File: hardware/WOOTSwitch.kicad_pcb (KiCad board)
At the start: 2 copper layers, 100 x 88 mm, 133 parts, among them J1 Mini-DIN-4-G, J10 POWSEL, J11 TWI, J12 TWI, J13 Mini-DIN-4-G, J14 Mini-DIN-4-G, J15 Mini-DIN-4-G, J16 Mini-DIN-4-G, J2 Mini-DIN-4-G, J7 Barrel_Jack_MountingPin, J8 EXT_POW, J9 SW1, Q1 MMBT3904, Q11 2N7002, Q15 2N7002, Q17 2N7002, Q18 2N7002, Q19 2N7002, Q2 MMBT3904, Q20 2N7002, Q21 2N7002, Q22 2N7002, Q23 2N7002, Q24 2N7002, Q25 2N7002, Q26 2N7002, Q27 2N7002, Q28 2N7002, Q29 2N7002, Q3 MMBT3904, Q30 2N7002, Q31 2N7002, Q32 2N7002, Q33 2N7002, Q34 2N7002, Q35 2N7002, Q36 2N7002, Q37 2N7002, Q38 2N7002, Q39 2N7002, Q4 MMBT3904, Q40 2N7002, Q5 MMBT3904, Q6 MMBT3904, Q8 MMBT3904, Q9 2N7002, SW2 1825910-6, U1 Pico, U2 LM1117-5.0

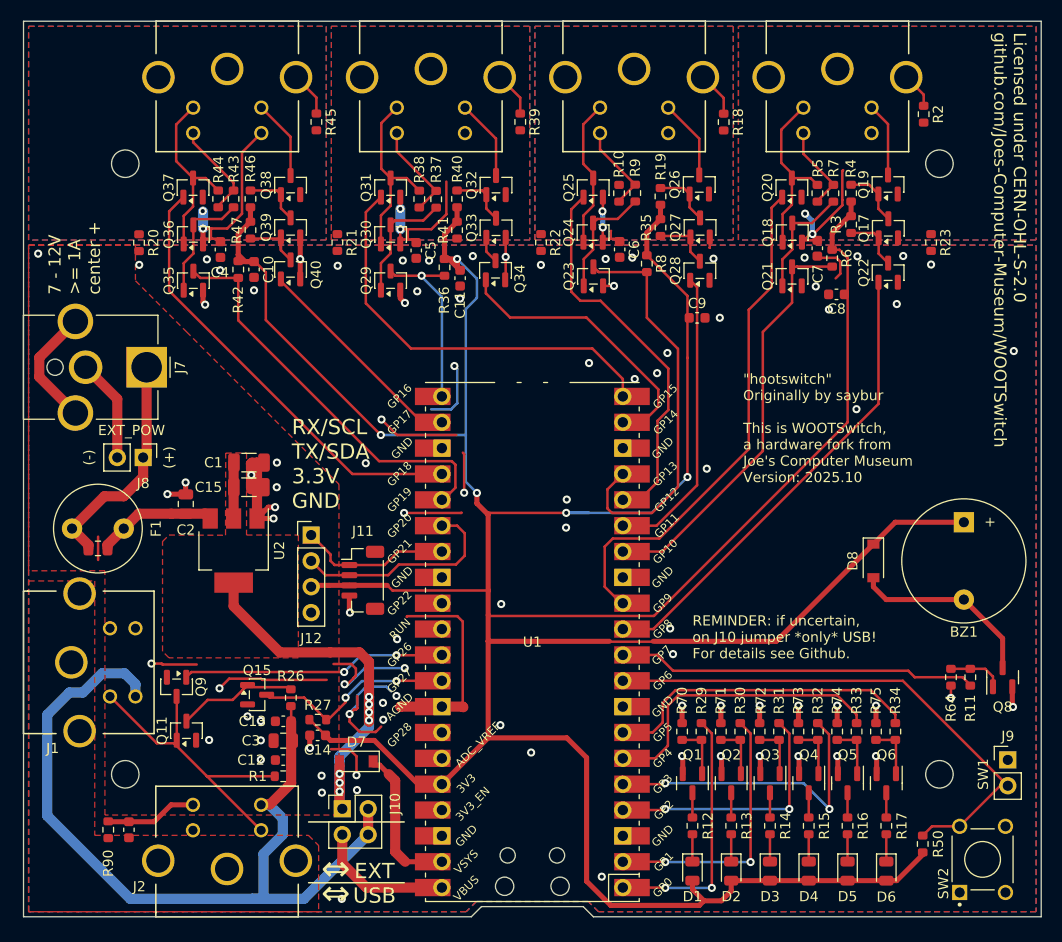
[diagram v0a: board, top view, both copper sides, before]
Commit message: Moved mounting holes
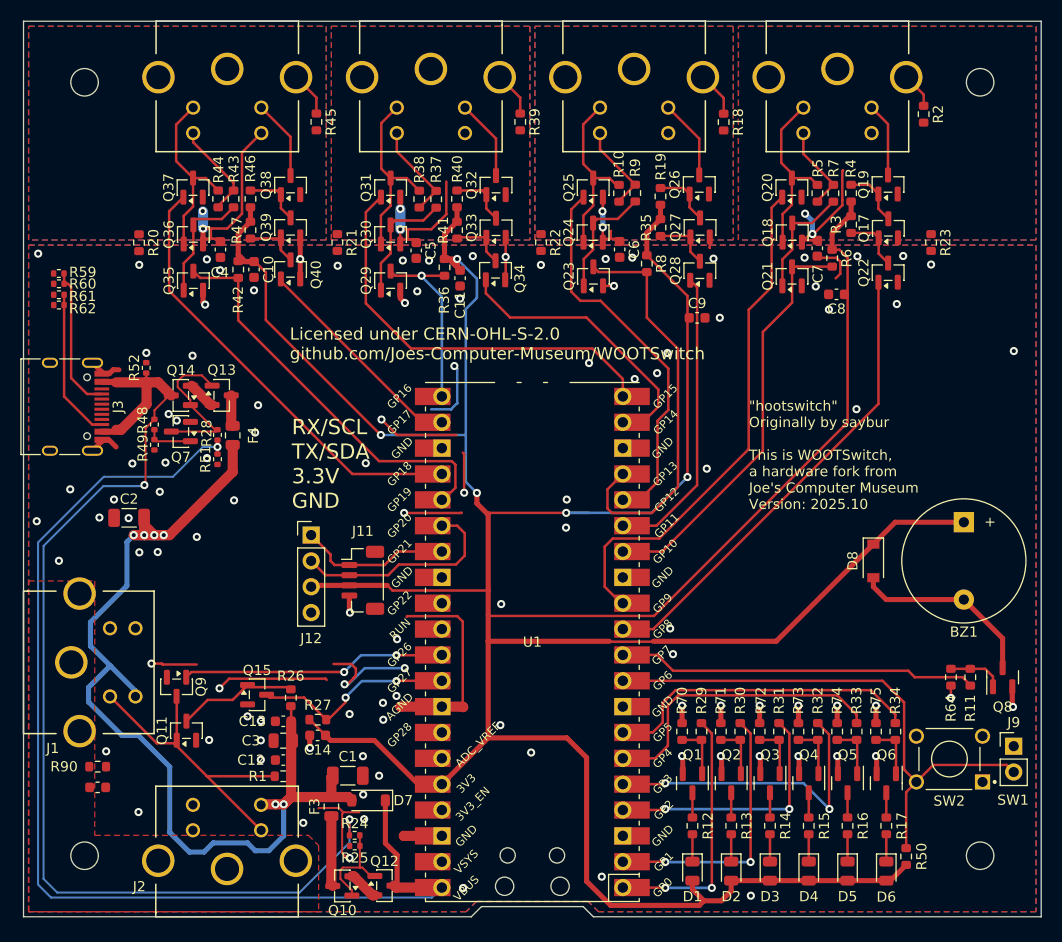
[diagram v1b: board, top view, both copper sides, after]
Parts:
- removed C15: 47uF, Capacitor_SMD:C_1206_3216Metric
- removed F1: 500mA, Fuse:Fuse_Littelfuse_372_D8.50mm
- removed F2: 500mA, Fuse:Fuse_0805_2012Metric
- removed J10: POWSEL, Connector_PinHeader_2.54mm:PinHeader_2x02_P2.54mm_Vertical
- removed J7: Barrel_Jack_MountingPin, Connector_BarrelJack:BarrelJack_CUI_PJ-063AH_Horizontal_CircularHoles
- removed J8: EXT_POW, Connector_PinHeader_2.54mm:PinHeader_1x02_P2.54mm_Vertical
- removed U2: LM1117-5.0, Package_TO_SOT_SMD:SOT-223-3_TabPin2
- added F3: 500mA, Fuse:Fuse_0805_2012Metric, F.Cu at (90.2, 137.2)
- added F4: 500mA, Fuse:Fuse_0805_2012Metric, F.Cu at (80.6, 100.7)
- added J3: USB_C_Receptacle, Connector_USB:USB_C_Receptacle_HRO_TYPE-C-31-M-12, F.Cu at (63.6, 97.9)
- added Q10: AO3401A, Package_TO_SOT_SMD:SOT-23, F.Cu at (91.3, 145.0)
- added Q12: AO3401A, Package_TO_SOT_SMD:SOT-23, F.Cu at (95.5, 144.9)
- added Q13: AO3401A, Package_TO_SOT_SMD:SOT-23, F.Cu at (79.5, 96.8)
- added Q14: AO3401A, Package_TO_SOT_SMD:SOT-23, F.Cu at (75.5, 96.8)
- added Q7: AO3400A, Package_TO_SOT_SMD:SOT-23, F.Cu at (75.5, 100.3)
- added R24: 100, Resistor_SMD:R_0402_1005Metric, F.Cu at (92.5, 140.0)
- added R25: 10k, Resistor_SMD:R_0402_1005Metric, F.Cu at (92.5, 141.0)
- added R28: 10k, Resistor_SMD:R_0402_1005Metric, F.Cu at (79.1, 100.7)
- added R48: 100, Resistor_SMD:R_0402_1005Metric, F.Cu at (72.9, 99.6)
- added R49: 10k, Resistor_SMD:R_0402_1005Metric, F.Cu at (72.9, 101.6)
- added R51: 1M, Resistor_SMD:R_0402_1005Metric, F.Cu at (79.1, 103.0)
- added R52: 1M, Resistor_SMD:R_0402_1005Metric, F.Cu at (72.1, 94.1)
- added R59: 10k, Resistor_SMD:R_0402_1005Metric, F.Cu at (63.5, 84.8)
- added R60: 10k, Resistor_SMD:R_0402_1005Metric, F.Cu at (63.5, 85.8)
- added R61: 10k, Resistor_SMD:R_0402_1005Metric, F.Cu at (63.5, 86.9)
- added R62: 10k, Resistor_SMD:R_0402_1005Metric, F.Cu at (63.5, 87.9)
- C10, C11, C8, C9: value 100N -> 100nF
- C2: value 10uF -> 47uF; footprint Capacitor_SMD:C_0805_2012Metric -> Capacitor_SMD:C_1206_3216Metric
- D7: value type="D" model="B5819W" lib="" -> B5819W
- R50: value 4K7 -> 4.7k
- moved C1 32.3 mm to (91.9, 134.1), turned to 180 degrees
- moved SW2 10.4 mm to (151.0, 132.5), turned to 180 degrees
- moved H1 8.94 mm to (66.0, 142.0)
- moved H2 8.94 mm to (66.0, 66.0)
- moved H3 8.94 mm to (154.0, 142.0)
- moved H4 8.94 mm to (154.0, 66.0)
- moved R90 6.28 mm to (67.3, 133.2), turned to 180 degrees
- moved C2 5.73 mm to (70.4, 108.8), turned to 0 degrees
- moved L1 5.18 mm to (67.3, 135.3), turned to 180 degrees
- moved D7 4.02 mm to (93.9, 136.6)
- moved R50 2.04 mm to (146.7, 142.1)
- moved J9 1.47 mm to (157.3, 131.2)
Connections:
- C1 pad 1: Net-(D7-A) -> GND
- C1 pad 2: GND -> +5V
- C2 pad 1: Net-(U2-VI) -> GND
- C2 pad 2: GND -> +5V
- D7 pad 1: Net-(D7-K) -> VBUS
- D7 pad 2: Net-(D7-A) -> +5V
- U1 pad 39: Net-(D7-K) -> VSYS
- U1 pad 40: Net-(J10-Pin_3) -> VBUS
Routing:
- net VBUS: track 0.00 -> 110.8 mm, vias 0 -> 1
- net USB_C_PWR: track 0.00 -> 109.6 mm, vias 0 -> 2
- net Net-(D7-A): track 46.0 -> 0.00 mm, vias 7 -> 0
- net GND: track 164.2 -> 139.6 mm, vias 90 -> 108
- net Net-(J8-Pin_1): track 22.6 -> 0.00 mm
- net +5V: track 86.0 -> 103.0 mm, vias 0 -> 6
- net Net-(U2-VI): track 15.2 -> 0.00 mm
- net Net-(Q13-G): track 0.00 -> 15.2 mm
- net Net-(J3-CC2): track 0.00 -> 14.8 mm
- net Net-(D7-K): track 14.8 -> 0.00 mm
- net Net-(J3-CC1): track 0.00 -> 14.5 mm
- net Net-(J10-Pin_3): track 13.6 -> 0.00 mm
- net (no net): track 11.9 -> 0.00 mm
- net Net-(J8-Pin_2): track 10.2 -> 0.00 mm
- net Net-(Q10-G): track 0.00 -> 9.99 mm
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- removed copper zone on F.Cu, net Net-(D7-A)
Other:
- board text removed: "(+)"
- board text removed: "(-)"
- board text removed: "7 - 12V >= 1A center +"
- board text removed: "EXT"
- board text removed: "REMINDER: if uncertain, on J10 jumper *only* USB! For details see Github."
- board text removed: "USB"
- board text removed: "⇔"
